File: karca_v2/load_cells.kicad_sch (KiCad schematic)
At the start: 18 parts, among them J4 LoadCell_1_2, J5 LoadCell_3_4, U2 NUP4202, U3 MCP3208, U4 NUP4202, U5 NUP4202, U6 TLV9304xD, U7 TLV9304xD

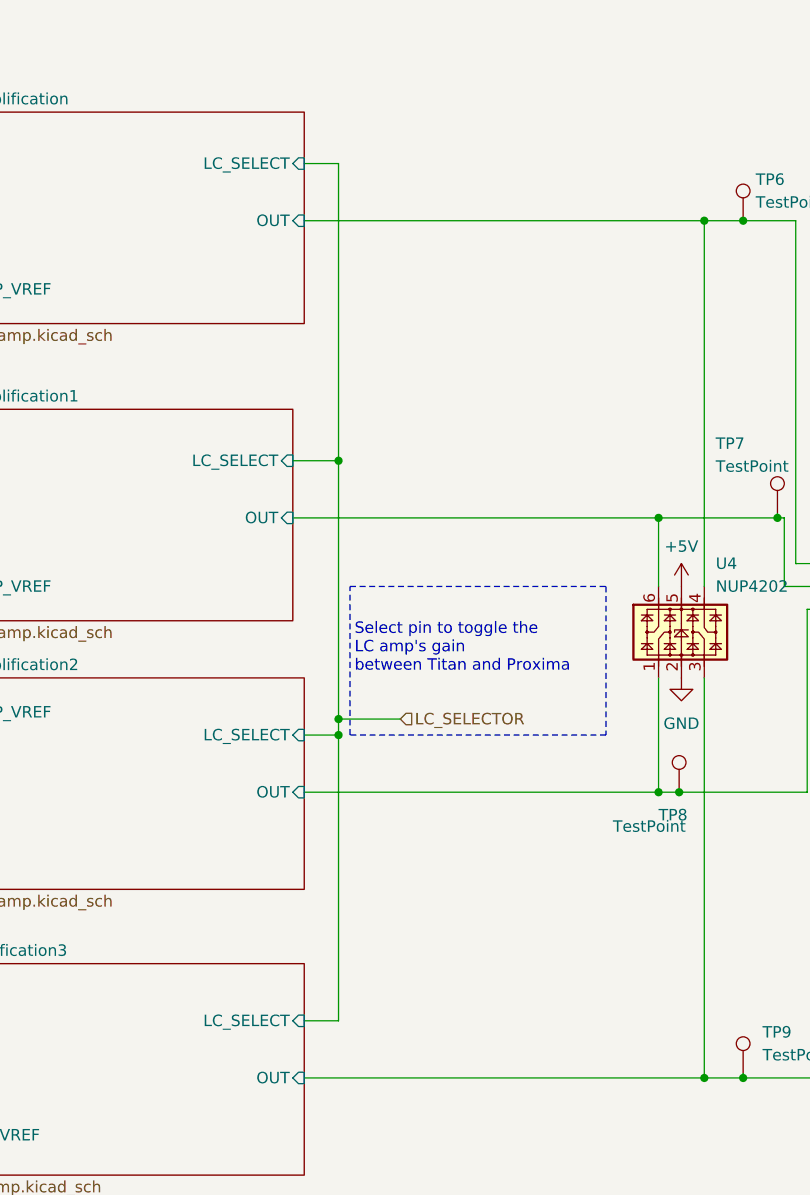
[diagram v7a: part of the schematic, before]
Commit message: replaced digital switches with jumpers, simpler design
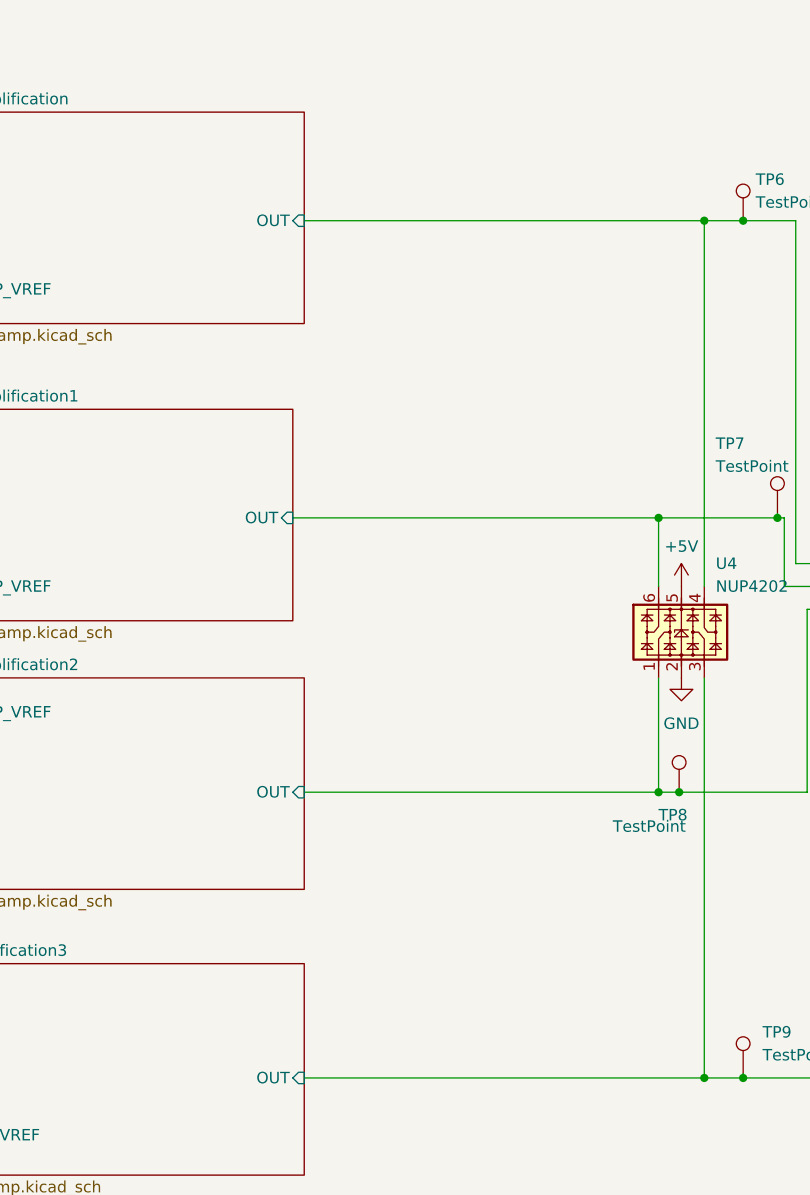
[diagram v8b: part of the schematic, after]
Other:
- sheet LC_Amplification ports: added none; removed LC_SELECT
- sheet LC_Amplification1 ports: added none; removed LC_SELECT
- sheet LC_Amplification2 ports: added none; removed LC_SELECT
- sheet LC_Amplification3 ports: added none; removed LC_SELECT
- note removed: "Select pin to toggle the LC amp's gain between Titan and Proxima"
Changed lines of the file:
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@@
   (junction (at 184.15 111.76) (diameter 0) (color 0 0 0 0)
   )
-  (junction (at 148.59 103.632) (diameter 0) (color 0 0 0 0)
-  )
   (junction (at 46.355 158.75) (diameter 0) (color 0 0 0 0)
   )
@@
   (junction (at 44.831 113.03) (diameter 0) (color 0 0 0 0)
   )
-  (junction (at 148.59 74.93) (diameter 0) (color 0 0 0 0)
-  )
   (junction (at 229.87 66.04) (diameter 0) (color 0 0 0 0)
   )
@@
   (junction (at 67.945 118.11) (diameter 0) (color 0 0 0 0)
   )
-  (junction (at 148.59 105.41) (diameter 0) (color 0 0 0 0)
-  )
   (junction (at 186.436 111.76) (diameter 0) (color 0 0 0 0)
   )
@@
     (stroke (width 0) (type default))
   )
-  (wire (pts (xy 148.59 103.632) (xy 148.59 105.41))
-    (stroke (width 0) (type default))
-  )
   (wire (pts (xy 193.548 143.002) (xy 193.548 143.51))
     (stroke (width 0) (type default))
@@
     (stroke (width 0) (type default))
   )
-  (wire (pts (xy 148.59 105.41) (xy 144.78 105.41))
-    (stroke (width 0) (type default))
-  )
   (wire (pts (xy 226.06 99.06) (xy 226.06 100.33))
     (stroke (width 0) (type default))
@@
     (stroke (width 0) (type default))
   )
-  (wire (pts (xy 148.59 41.91) (xy 144.78 41.91))
-    (stroke (width 0) (type default))
-  )
   (wire (pts (xy 32.385 53.34) (xy 36.195 53.34))
     (stroke (width 0) (type default))
@@
     (stroke (width 0) (type default))
   )
-  (wire (pts (xy 155.448 103.632) (xy 148.59 103.632))
-    (stroke (width 0) (type default))
-  )
   (wire (pts (xy 60.325 40.64) (xy 67.31 40.64))
     (stroke (width 0) (type default))
@@
     (stroke (width 0) (type default))
   )
-  (wire (pts (xy 148.59 137.16) (xy 144.78 137.16))
-    (stroke (width 0) (type default))
-  )
-  (wire (pts (xy 148.59 105.41) (xy 148.59 137.16))
-    (stroke (width 0) (type default))
-  )
   (wire (pts (xy 144.78 143.51) (xy 189.23 143.51))
     (stroke (width 0) (type default))
@@
     (stroke (width 0) (type default))
   )
-  (wire (pts (xy 148.59 74.93) (xy 148.59 103.632))
-    (stroke (width 0) (type default))
-  )
   (wire (pts (xy 96.52 115.57) (xy 96.52 106.68))
     (stroke (width 0) (type default))
   )
-  (wire (pts (xy 143.51 74.93) (xy 148.59 74.93))
-    (stroke (width 0) (type default))
-  )
   (wire (pts (xy 66.675 43.18) (xy 66.675 46.99))
     (stroke (width 0) (type default))
@@
     (stroke (width 0) (type default))
   )
-  (wire (pts (xy 148.59 41.91) (xy 148.59 74.93))
-    (stroke (width 0) (type default))
-  )
   (wire (pts (xy 65.405 43.18) (xy 65.405 62.23))
     (stroke (width 0) (type default))
@@
   (wire (pts (xy 65.405 72.39) (xy 65.405 77.47))
     (stroke (width 0) (type default))
-  )
-  (rectangle (start 149.86 88.9) (end 178.308 105.41)
-    (stroke (width 0) (type dash))
-    (fill (type none))
-  )
-  (text "Select pin to toggle the\nLC amp's gain \nbetween Titan and Proxima "
-    (at 150.368 98.552 0)
-    (effects (font (size 1.27 1.27)) (justify left bottom))
   )
   (label "IN_AMP_VREF" (at 104.14 88.9 180) (fields_autoplaced)
@@
   (hierarchical_label "TC_3_ADC" (shape input) (at 213.36 76.2 180) (fields_autoplaced)
     (effects (font (size 1.27 1.27)) (justify right))
-  )
-  (hierarchical_label "LC_SELECTOR" (shape input) (at 155.448 103.632 0) (fields_autoplaced)
-    (effects (font (size 1.27 1.27)) (justify left))
   )
   (hierarchical_label "LC_MOSI" (shape input) (at 243.84 86.36 0) (fields_autoplaced)
@@
       (effects (font (size 1.27 1.27)) (justify left))
     )
-    (pin "LC_SELECT" input (at 144.78 41.91 0)
-      (effects (font (size 1.27 1.27)) (justify right))
-    )
     (pin "INAMP_VREF" input (at 104.14 55.88 180)
       (effects (font (size 1.27 1.27)) (justify left))
@@
       (effects (font (size 1.27 1.27)) (justify left))
     )
-    (pin "LC_SELECT" input (at 143.51 74.93 0)
-      (effects (font (size 1.27 1.27)) (justify right))
-    )
     (pin "INAMP_VREF" input (at 104.14 88.9 180)
       (effects (font (size 1.27 1.27)) (justify left))
@@
       (effects (font (size 1.27 1.27)) (justify left))
     )
-    (pin "LC_SELECT" input (at 144.78 105.41 0)
-      (effects (font (size 1.27 1.27)) (justify right))
-    )
     (pin "INAMP_VREF" input (at 104.14 102.87 180)
       (effects (font (size 1.27 1.27)) (justify left))
@@
       (effects (font (size 1.27 1.27)) (justify left))
     )
-    (pin "LC_SELECT" input (at 144.78 137.16 0)
-      (effects (font (size 1.27 1.27)) (justify right))
-    )
     (pin "INAMP_VREF" input (at 102.87 149.86 180)
